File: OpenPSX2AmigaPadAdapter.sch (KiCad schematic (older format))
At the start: 39 parts, among them J1 TO_PSX_PAD, J2 DB9_F, J3 CONN_FTDI, J4 CONN_ICSP, J99 OSHW_LOGO, Q1 BSS138, Q2 BSS138, Q3 BSS138, Q4 BSS138, SW1 RESET, U1 ATmega328P-AU, U2 LM1117-3.3, Y1 16M, Y2 16M

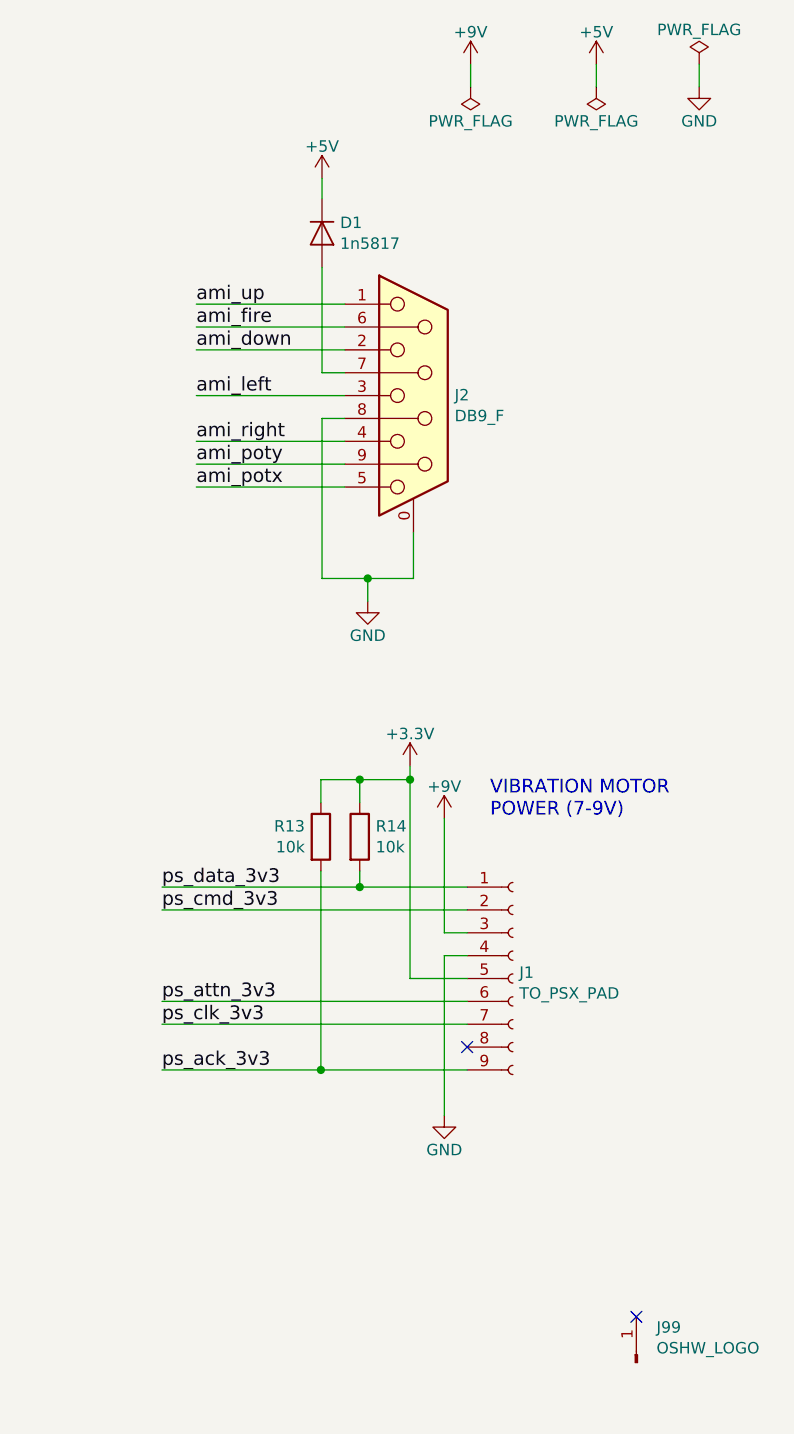
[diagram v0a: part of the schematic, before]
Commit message: Remove pull-up on ACK. Add on B1/B2 outputs.
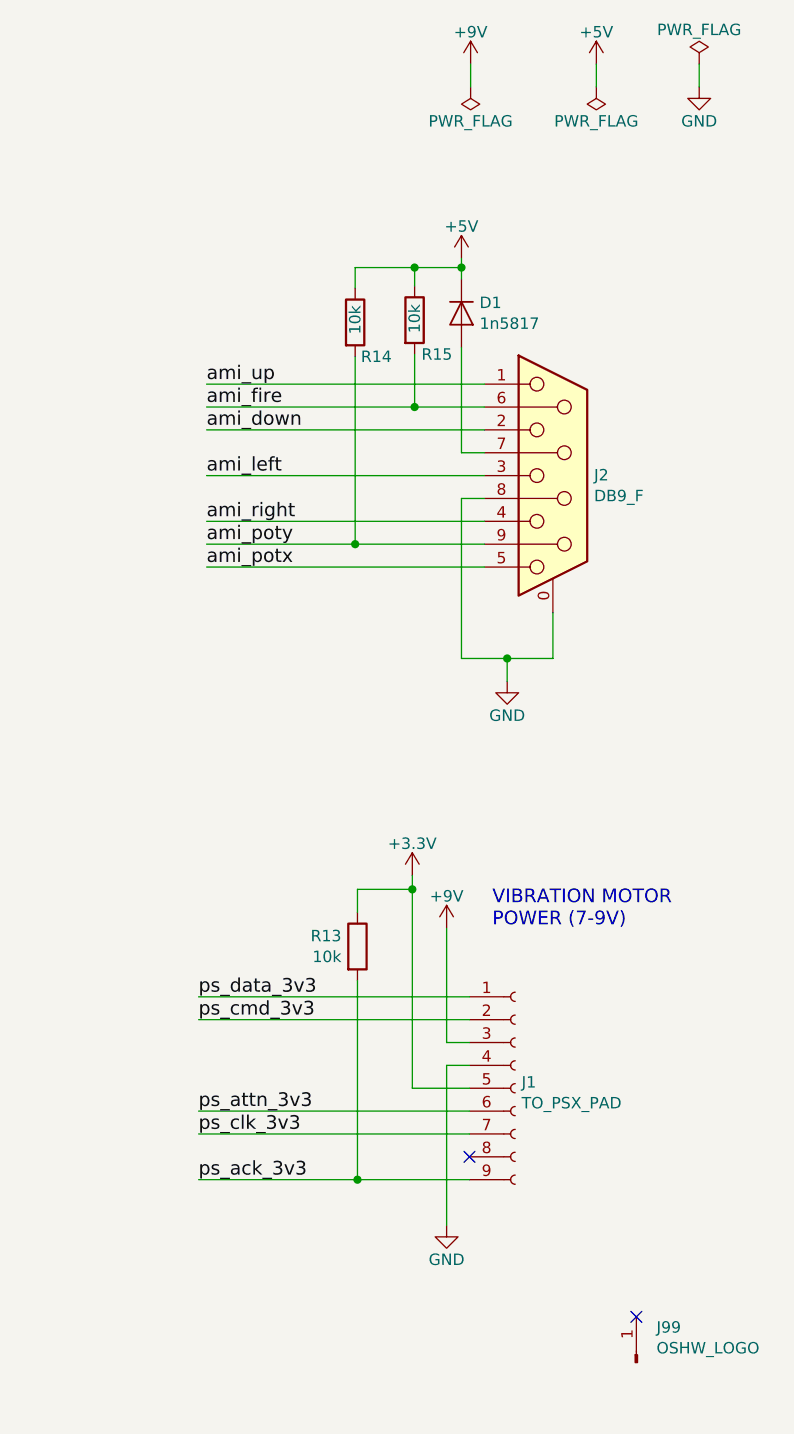
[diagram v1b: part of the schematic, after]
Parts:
- added R15: 10k, Resistor_SMD:R_0805_2012Metric_Pad1.15x1.40mm_HandSolder, symbol Device:R
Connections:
- wire segments 177 -> 182
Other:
- moved on the sheet: D1, J1, J2, R13

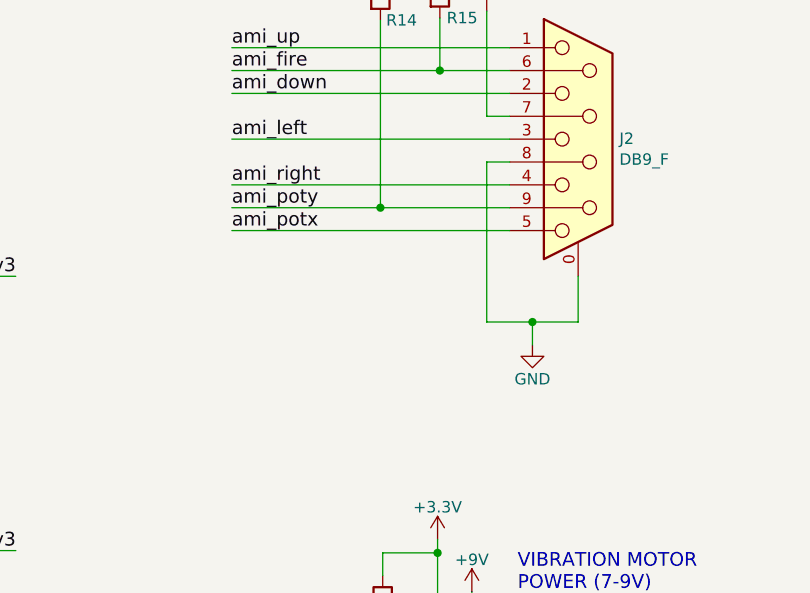
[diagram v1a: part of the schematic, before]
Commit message: Add capacitor on potx/y as per original CD32 controller
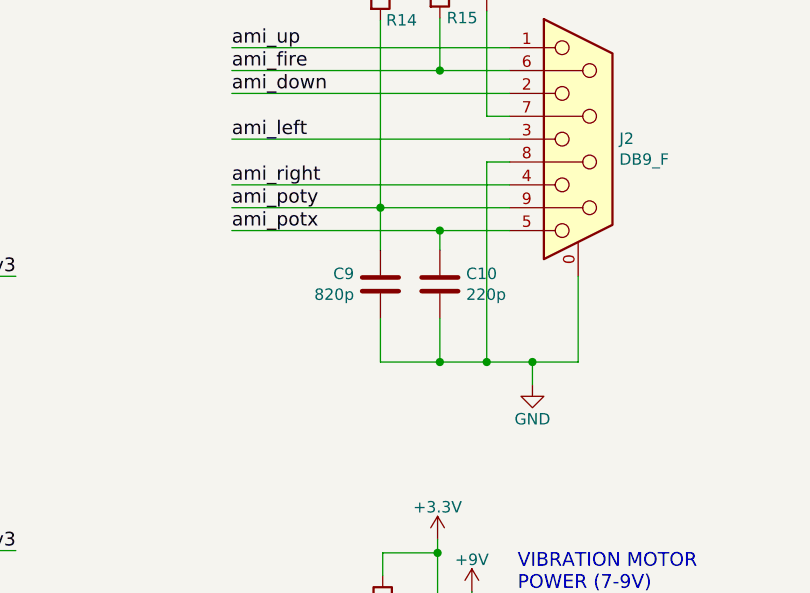
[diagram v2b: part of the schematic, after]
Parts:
- added C10: 220p, Capacitor_SMD:C_0805_2012Metric_Pad1.15x1.40mm_HandSolder, symbol Device:C
- added C9: 820p, Capacitor_SMD:C_0805_2012Metric_Pad1.15x1.40mm_HandSolder, symbol Device:C
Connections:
- wire segments 182 -> 189
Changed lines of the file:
@@
 L power:GND #PWR02
 U 1 1 5D18C393
-P 10060 3500
-F 0 "#PWR02" H 10060 3250 50  0001 C CNN
-F 1 "GND" H 10060 3350 50  0000 C CNN
-F 2 "" H 10060 3500 50  0001 C CNN
-F 3 "" H 10060 3500 50  0001 C CNN
-	1    10060 3500
+P 10060 3675
+F 0 "#PWR02" H 10060 3425 50  0001 C CNN
+F 1 "GND" H 10060 3525 50  0000 C CNN
+F 2 "" H 10060 3675 50  0001 C CNN
+F 3 "" H 10060 3675 50  0001 C CNN
+	1    10060 3675
 	1    0    0    -1
 $EndComp
@@
 	9960 2900 9395 2900
 Wire Wire Line
-	9960 3000 8745 3000
-Wire Wire Line
-	9860 2700 9860 3400
-Wire Wire Line
-	9860 3400 10060 3400
-Wire Wire Line
-	10260 3400 10260 3200
-Connection ~ 10060 3400
-Wire Wire Line
-	10060 3500 10060 3400
+	9960 3000 9655 3000
+Wire Wire Line
+	9860 2700 9860 3575
+Wire Wire Line
+	9860 3575 10060 3575
+Wire Wire Line
+	10260 3575 10260 3200
+Connection ~ 10060 3575
+Wire Wire Line
+	10060 3675 10060 3575
 Wire Wire Line
 	9860 2700 9960 2700
@@
 Connection ~ 2010 6555
 Wire Wire Line
-	10060 3400 10260 3400
+	10060 3575 10260 3575
 Wire Wire Line
 	2010 5905 2010 6055
@@
 Wire Wire Line
 	9395 2900 8745 2900
+$Comp
+L Device:C C10
+U 1 1 5DB50106
+P 9655 3235
+F 0 "C10" H 9770 3281 50  0000 L CNN
+F 1 "220p" H 9770 3190 50  0000 L CNN
+F 2 "Capacitor_SMD:C_0805_2012Metric_Pad1.15x1.40mm_HandSolder" H 9693 3085 50  0001 C CNN
+F 3 "~" H 9655 3235 50  0001 C CNN
+	1    9655 3235
+	1    0    0    -1
+$EndComp
+$Comp
+L Device:C C9
+U 1 1 5DB5B8E8
+P 9395 3235
+F 0 "C9" H 9280 3281 50  0000 R CNN
+F 1 "820p" H 9280 3190 50  0000 R CNN
+F 2 "Capacitor_SMD:C_0805_2012Metric_Pad1.15x1.40mm_HandSolder" H 9433 3085 50  0001 C CNN
+F 3 "~" H 9395 3235 50  0001 C CNN
+	1    9395 3235
+	1    0    0    -1
+$EndComp
+Wire Wire Line
+	9395 3085 9395 2900
+Wire Wire Line
+	9655 3085 9655 3000
+Connection ~ 9655 3000
+Wire Wire Line
+	9655 3000 8745 3000
+Wire Wire Line
+	9655 3385 9655 3575
+Wire Wire Line
+	9655 3575 9860 3575
+Connection ~ 9860 3575
+Wire Wire Line
+	9395 3385 9395 3575
+Wire Wire Line
+	9395 3575 9655 3575
+Connection ~ 9655 3575
 $EndSCHEMATC
